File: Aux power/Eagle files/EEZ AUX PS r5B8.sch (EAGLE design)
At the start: 74 parts, among them IC1 LM25575, IC2 MC7812, IC3 TPD4E002DRLR, IC4 TPD2E001DZDR, IC5 ADUM3160BRWZ, Q1 BTA26-600, Q2 BTA26-600, Q3 IRLL014N, X1 282836-5, X2 09185067324, X3 22-23-2031, X4 LMJ2138812S0LOT6C, X5 826629-8, X6 826629-5, X7 SSW-105-02-S-S, X8 2411-01

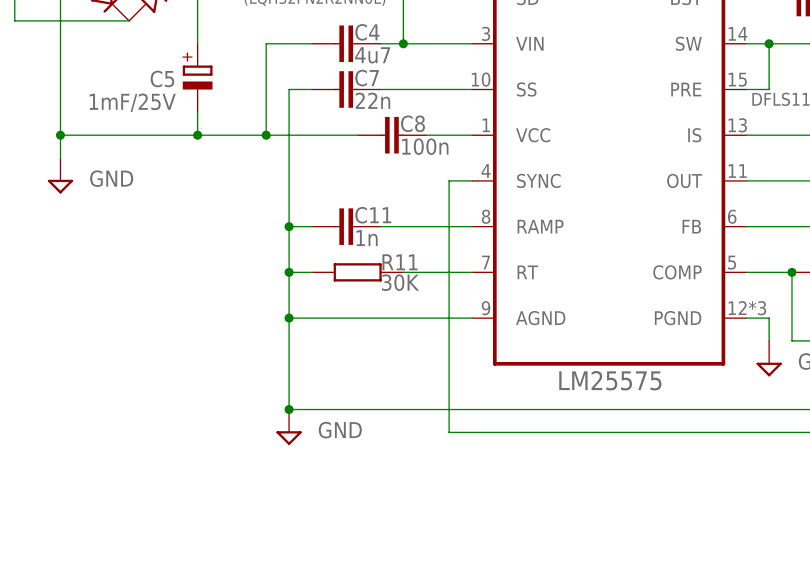
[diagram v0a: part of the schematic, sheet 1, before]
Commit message: Rt value corrections for AUX PS and Power board
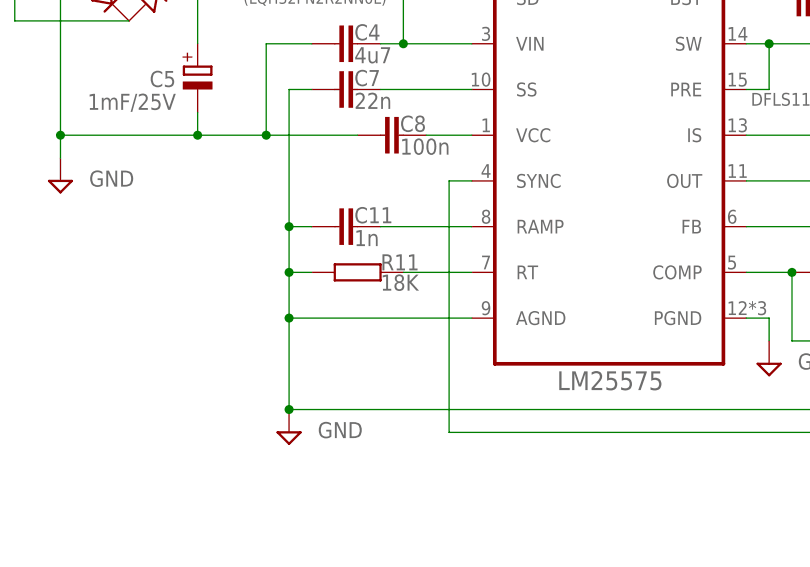
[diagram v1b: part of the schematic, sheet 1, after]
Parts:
- R11: value 30K -> 18K
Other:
- note removed: "Note 1.1: replace with 33K or 36K (to decrease frequency) if sync with power board is required"
- note removed: "See note 1.1"
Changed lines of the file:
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@@
 <part name="B1" library="rectifier" deviceset="DF*S" device="" technology="01" value="DF01S"/>
 <part name="C11" library="rcl" deviceset="C-EU" device="C0805" value="1n"/>
-<part name="R11" library="rcl" deviceset="R-EU_" device="R0805" value="30K"/>
+<part name="R11" library="rcl" deviceset="R-EU_" device="R0805" value="18K"/>
 <part name="R12" library="rcl" deviceset="R-EU_" device="R0805" value="20K"/>
 <part name="C12" library="rcl" deviceset="C-EU" device="C0805" value="3n9"/>
@@
 <text x="164.465" y="29.845" size="2.54" layer="94" font="vector">AC input protection, in-rush current limiter</text>
 <text x="164.465" y="26.035" size="2.54" layer="94" font="vector">+5V/1A power supply</text>
-<text x="6.985" y="15.24" size="1.27" layer="103">Note 1.1: replace with 33K or 36K (to decrease frequency) if sync with power board is required</text>
-<text x="92.71" y="55.88" size="1.27" layer="103">See note 1.1</text>
 <text x="12.7" y="165.735" size="1.778" layer="97" rot="R180">Line in</text>
 <text x="12.7" y="138.43" size="1.778" layer="97" rot="R180">Neutral in</text>

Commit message: AUX PS renumbering
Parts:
- removed R17: 5K6, rcl:R-EU_R0805
- removed R18: 10K, rcl:R-EU_R0805
- removed X1: 282836-5, EEZ_Lib1:TBLOCK5.0_5A
- removed X2: 09185067324, EEZ_Lib1:IDC-10PINBLACK
- removed X3: 22-23-2031, con-molex:22-23-2031
- added C97: 10u, MyLib6:ECAPPANASONIC_C
- added D21: BAS316, diode:DIODE-SOD323-W
- added R118: 5K6, rcl:R-EU_R0805
- added R119: 10K, rcl:R-EU_R0805
- added X10, X9: 826629-5, con-samtec:SSW-105-02-S-S
- added X11: 2411-01, con-kycon:KUSBVX-BS1N
- FB6, FB7: value 2506033007Y3 -> 60R@100MHz
- TR2: value TEZ6/D230/15V -> TEZ6/D230/12V
- X4: value LMJ2138812S0LOT6C -> 282836-5; device EEZ_Lib1:RJ45-VERT -> EEZ_Lib1:TBLOCK5.0_5A
- X5: value 826629-8 -> 09185067324; device con-samtec:SSW-108-02-S-S -> EEZ_Lib1:IDC-10PINBLACK; TME (none) -> T821-1-10-S1
- X6: value 826629-5 -> 22-23-2031; device con-samtec:SSW-105-02-S-S -> con-molex:22-23-2031
- X7: value SSW-105-02-S-S -> LMJ2138812S0LOT6C; device con-samtec:SSW-105-02-S-S -> EEZ_Lib1:RJ45-VERT
- X8: value 2411-01 -> 826629-8; device con-kycon:KUSBVX-BS1N -> con-samtec:SSW-108-02-S-S
- renumbered C1 to C84, C10 to C93, C11 to C94, C12 to C95, C13 to C96, C14 to C98, C15 to C99, C16 to C100, C17 to C101, C18 to C102, C19 to C103, C2 to C85, C20 to C104, C3 to C86, C4 to C87, C5 to C88, C6 to C89, C7 to C90, C8 to C91, C9 to C92, D1 to D19, D2 to D20, IC1 to IC16, IC2 to IC17, IC3 to IC18, IC4 to IC19, IC5 to IC20, L1 to L8, L2 to L9, L3 to FB5, L4 to L10, L5 to FB6, L6 to FB7, Q1 to Q20, Q2 to Q21, Q3 to Q22, R1 to R102, R10 to R111, R11 to R112, R12 to R113, R13 to R114, R14 to R115, R15 to R116, R16 to R117, R19 to R120, R2 to R103, R20 to R121, R3 to R104, R4 to R105, R5 to R106, R6 to R107, R7 to R108, R8 to R109, R9 to R110, TR1 to TR2, ZD1 to ZD6, ZD2 to ZD7
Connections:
- net DC_PREG1 renamed DC_PREG2
- net IS renamed IS1
- net SW renamed SW2
- removed net +3V3: FB5.2, X5-8.1
- removed net AC_IN1: C84.1, Q20.A1, Q21.A1, TR2.P2, VAR1.P$2, X1-1.1, ZD7.2
- removed net AC_IN2: C84.2, C85.1, TR2.P1, VAR2.P$1, X1-2.1, X1-4.1, ZD6.2
- removed net ETH_ACTLED: X4.YELLOW_A, X5-2.1
- removed net ETH_IN+: IC18.IO4, X4.RD-, X5-4.1
- removed net ETH_IN-: IC18.IO3, X4.RD+, X5-5.1
- removed net ETH_LINKLED: X4.GREEN-A, X5-1.1
- removed net ETH_OUT+: IC18.IO2, X4.TD-, X5-6.1
- removed net ETH_OUT-: IC18.IO1, X4.TD+, X5-7.1
- removed net FAN_CONTROL: R115.2, X2-6.1
- removed net FAN_SENSE: R17.2, R18.1, X2-5.1, X3-3.S
- removed net N$11: Q21.A2, R102.2, R103.2, R105.1, X1-3.1
- removed net N$13: IC16.SYNC, X2-7.1
- removed net N$21: C98.-, L10.1, X3-2.S
- removed net PWR_DIRECT: R104.2, X2-3.1
- removed net PWR_SSTART: R107.2, X2-4.1
- new net AC_IN1_MAIN: C84.1, Q20.A1, Q21.A1, TR2.P2, VAR1.P$2, X4-1.1, ZD7.2
- new net AC_IN2_MAIN: C84.2, C85.1, TR2.P1, VAR2.P$1, X4-2.1, X4-4.1, ZD6.2
- new net AUX_+3V3: FB5.2, X8-8.1
- new net AUX_ETH_ACTLED: X7.YELLOW_A, X8-2.1
- new net AUX_ETH_IN+: IC18.IO4, X7.RD-, X8-4.1
- new net AUX_ETH_IN-: IC18.IO3, X7.RD+, X8-5.1
- new net AUX_ETH_LINKLED: X7.GREEN-A, X8-1.1
- new net AUX_ETH_OUT+: IC18.IO2, X7.TD-, X8-6.1
- new net AUX_ETH_OUT-: IC18.IO1, X7.TD+, X8-7.1
- new net AUX_FAN_CTRL: R115.2, X5-6.1
- new net AUX_FAN_SENSE: D21.A, R118.2, R119.1, X5-5.1
- new net AUX_PWR_DIRECT: R104.2, X5-3.1
- new net AUX_PWR_SSTART: R107.2, X5-4.1
- new net N$163: D21.C, X6-3.S
- new net N$68: IC16.SYNC, X5-7.1
- new net N$82: Q21.A2, R102.2, R103.2, R105.1, X4-3.1
- new net N$86: C98.-, L10.1, X6-2.S
- net +5V: now also R118.1, X5-10.1, X5-8.1; no longer R17.1, X2-10.1, X2-8.1
- net 12VDC: now also C97.+, X6-1.S; no longer X3-1.S
- net AC_EARTH: now also X11.S1, X11.S2, X4-5.1, X7.SH, X9-5.1; no longer X1-5.1, X4.SH, X6-5.1, X8.S1, X8.S2
- net D+: now also X11.3, X9-3.1; no longer X6-3.1, X8.3
- net D-: now also X11.2, X9-2.1; no longer X6-2.1, X8.2
- net GND: now also C97.-, R119.2, X5-1.1, X5-2.1, X5-9.1, X7.GREEN-C, X7.YELLOW-C; no longer R18.2, X2-1.1, X2-2.1, X2-9.1, X4.GREEN-C, X4.YELLOW-C
- net MCU_D+: now also X10-3.1; no longer X7-3.1
- net MCU_D-: now also X10-2.1; no longer X7-2.1
- net N$125: now also X7.CT; no longer X4.CT
- net XUSB_GND: now also X11.4, X9-4.1; no longer X6-4.1, X8.4
- net XUSB_VBUS: now also X11.1, X9-1.1; no longer X6-1.1, X8.1
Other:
- note added: "10-pin IDC connector X5"
- note added: "3-pin connector X6"
- note added: "5-pin connector X9, X10"
- note added: "5-pin power connector X4"
- note added: "8-pin connector X8"
- note added: "Digikey: 237-1085-ND"
- note added: "Fan+ (Red) 1"
- note added: "Fan- (Black) 2"
- note added: "Mouser: 553-VPP24-210"
- note added: "Newark: 93F8764"
- note removed: "10-pin IDC connector X2"
- note removed: "3-pin connector X4"
- note removed: "5-pin connector X6, X7"
- note removed: "5-pin power connector X1"
- note removed: "8-pin connector X5"
- note removed: "Digikey: 237-1086-ND"
- note removed: "Fan + (Red) 1"
- note removed: "Fan - (Black) 2"
- note removed: "Mouser: 553-VPP28-180"
- note removed: "Newark: 37B9209"

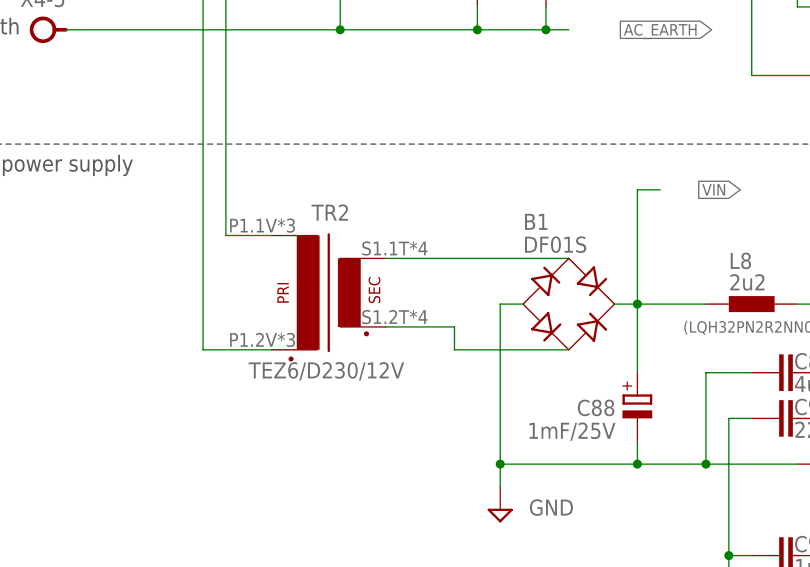
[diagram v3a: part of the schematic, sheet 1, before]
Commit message: Myrra AC/DC module for 115VAC, BOM updated
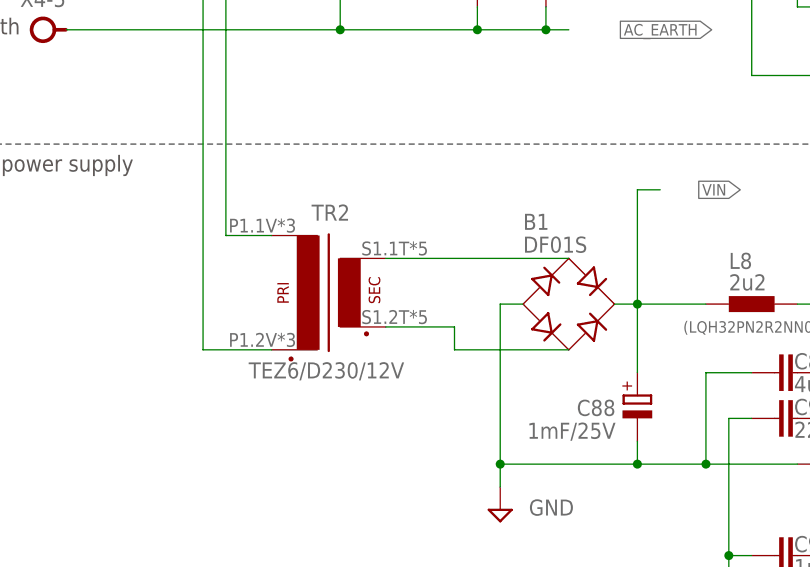
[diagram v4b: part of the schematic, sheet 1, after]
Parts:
- TR2: device EEZ_Lib1:PCB_TRAFO6VA_TEZ+VPP -> EEZ_Lib1:PCB_TRAFO6VA_TEZ+VPP+MYRRA
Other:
- note added: "Farnell: 2469211"
- note added: "Myrra 47202"
- note added: "TR2"
- note added: "VPP24-210"
- note added: "or AC/DC module"
- note removed: "TR1"
- note removed: "VPP28-180"
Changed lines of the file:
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@@
 <part name="R119" library="rcl" deviceset="R-EU_" device="R0805" value="10K"/>
 <part name="SUPPLY51" library="supply2" deviceset="GND" device=""/>
-<part name="TR2" library="EEZ_Lib1" deviceset="PCB_TRAFO6VA_TEZ+VPP" device="" value="TEZ6/D230/12V"/>
+<part name="TR2" library="EEZ_Lib1" deviceset="PCB_TRAFO6VA_TEZ+VPP" device="+MYRRA" value="TEZ6/D230/12V"/>
 <part name="VAR1" library="EEZ_Lib1" deviceset="VARISTOR" device="" value="S20K250"/>
 <part name="VAR2" library="EEZ_Lib1" deviceset="VARISTOR" device="" value="S20K250"/>
@@
 <text x="6.985" y="176.53" size="1.778" layer="97" rot="MR180">AC input protection and soft-start/stand-by</text>
 <text x="10.16" y="157.48" size="1.778" layer="103">AC input (230V)</text>
-<text x="9.525" y="34.925" size="1.6764" layer="103">SAR1</text>
-<text x="9.525" y="24.765" size="1.6764" layer="103">VAR1, VAR2</text>
-<text x="9.525" y="22.225" size="1.6764" layer="103">ZD1, ZD2</text>
-<text x="44.45" y="38.1" size="1.6764" layer="103">Code</text>
-<text x="26.67" y="38.1" size="1.6764" layer="103">Value</text>
-<text x="26.67" y="34.925" size="1.6764" layer="103">2027-23-BLF</text>
-<text x="44.45" y="34.925" size="1.6764" layer="103">Farnell: 1780455, TME: CG2-230L</text>
-<text x="26.67" y="24.765" size="1.6764" layer="103">S20K140</text>
-<text x="26.67" y="32.385" size="1.6764" layer="103">VPP28-180</text>
-<text x="44.45" y="27.305" size="1.6764" layer="103">Newark: 93F8764</text>
-<text x="44.45" y="24.765" size="1.6764" layer="103">Farnell: 1004387, TME: SIOV-S20K140</text>
-<wire x1="7.62" y1="40.64" x2="25.4" y2="40.64" width="0.1524" layer="103"/>
-<wire x1="25.4" y1="40.64" x2="43.18" y2="40.64" width="0.1524" layer="103"/>
-<wire x1="43.18" y1="40.64" x2="87.63" y2="40.64" width="0.1524" layer="103"/>
-<wire x1="87.63" y1="40.64" x2="87.63" y2="37.465" width="0.1524" layer="103"/>
-<wire x1="87.63" y1="37.465" x2="87.63" y2="21.59" width="0.1524" layer="103"/>
-<wire x1="87.63" y1="21.59" x2="43.18" y2="21.59" width="0.1524" layer="103"/>
-<wire x1="43.18" y1="21.59" x2="25.4" y2="21.59" width="0.1524" layer="103"/>
-<wire x1="25.4" y1="21.59" x2="7.62" y2="21.59" width="0.1524" layer="103"/>
-<wire x1="7.62" y1="21.59" x2="7.62" y2="37.465" width="0.1524" layer="103"/>
-<wire x1="7.62" y1="37.465" x2="7.62" y2="40.64" width="0.1524" layer="103"/>
-<wire x1="25.4" y1="21.59" x2="25.4" y2="40.64" width="0.1524" layer="103"/>
-<wire x1="43.18" y1="21.59" x2="43.18" y2="40.64" width="0.1524" layer="103"/>
-<wire x1="7.62" y1="37.465" x2="87.63" y2="37.465" width="0.1524" layer="103"/>
-<text x="9.525" y="38.1" size="1.6764" layer="103">Name</text>
-<text x="6.985" y="41.91" size="1.6764" layer="103">115VAC option:</text>
-<text x="9.525" y="32.385" size="1.6764" layer="103">TR1</text>
-<text x="26.67" y="22.225" size="1.6764" layer="103">1.5KE200CA</text>
-<text x="44.45" y="22.225" size="1.6764" layer="103">Farnell: 1837117, TME: 1.5KE200CA</text>
-<text x="44.45" y="32.385" size="1.6764" layer="103">Digikey: 237-1085-ND</text>
-<text x="44.45" y="29.845" size="1.6764" layer="103">Mouser: 553-VPP24-210</text>
 <circle x="232.41" y="67.31" radius="0.635" width="0.1524" layer="101"/>
 <circle x="232.41" y="69.85" radius="0.635" width="0.1524" layer="101"/>
@@
 <text x="2.54" y="152.4" size="1.4224" layer="103">or Schurter KM00.1105.11 IEC intlet</text>
 <text x="2.54" y="149.86" size="1.4224" layer="103">with Schurter 4301.1403 fuse drawer</text>
+<text x="6.985" y="34.925" size="1.6764" layer="103">SAR1</text>
+<text x="6.985" y="19.685" size="1.6764" layer="103">VAR1, VAR2</text>
+<text x="6.985" y="17.145" size="1.6764" layer="103">ZD1, ZD2</text>
+<text x="44.45" y="38.1" size="1.6764" layer="103">Code</text>
+<text x="24.13" y="38.1" size="1.6764" layer="103">Value</text>
+<text x="24.13" y="34.925" size="1.6764" layer="103">2027-23-BLF</text>
+<text x="44.45" y="34.925" size="1.6764" layer="103">Farnell: 1780455, TME: CG2-230L</text>
+<text x="24.13" y="19.685" size="1.6764" layer="103">S20K140</text>
+<text x="24.13" y="32.385" size="1.6764" layer="103">VPP24-210</text>
+<text x="44.45" y="19.685" size="1.6764" layer="103">Farnell: 1004387, TME: SIOV-S20K140</text>
+<wire x1="5.08" y1="40.64" x2="22.86" y2="40.64" width="0.1524" layer="103"/>
+<wire x1="22.86" y1="40.64" x2="43.18" y2="40.64" width="0.1524" layer="103"/>
+<wire x1="43.18" y1="40.64" x2="87.63" y2="40.64" width="0.1524" layer="103"/>
+<wire x1="87.63" y1="40.64" x2="87.63" y2="37.465" width="0.1524" layer="103"/>
+<wire x1="87.63" y1="37.465" x2="87.63" y2="16.51" width="0.1524" layer="103"/>
+<wire x1="87.63" y1="16.51" x2="43.18" y2="16.51" width="0.1524" layer="103"/>
+<wire x1="43.18" y1="16.51" x2="22.86" y2="16.51" width="0.1524" layer="103"/>
+<wire x1="22.86" y1="16.51" x2="5.08" y2="16.51" width="0.1524" layer="103"/>
+<wire x1="5.08" y1="16.51" x2="5.08" y2="37.465" width="0.1524" layer="103"/>
+<wire x1="5.08" y1="37.465" x2="5.08" y2="40.64" width="0.1524" layer="103"/>
+<wire x1="22.86" y1="16.51" x2="22.86" y2="40.64" width="0.1524" layer="103"/>
+<wire x1="43.18" y1="16.51" x2="43.18" y2="40.64" width="0.1524" layer="103"/>
+<wire x1="5.08" y1="37.465" x2="87.63" y2="37.465" width="0.1524" layer="103"/>
+<text x="6.985" y="38.1" size="1.6764" layer="103">Name</text>
+<text x="4.445" y="41.91" size="1.6764" layer="103">115VAC option:</text>
+<text x="6.985" y="32.385" size="1.6764" layer="103">TR2</text>
+<text x="24.13" y="17.145" size="1.6764" layer="103">1.5KE200CA</text>
+<text x="44.45" y="17.145" size="1.6764" layer="103">Farnell: 1837117, TME: 1.5KE200CA</text>
+<text x="44.45" y="22.225" size="1.6764" layer="103">Farnell: 2469211</text>
+<text x="44.45" y="32.385" size="1.6764" layer="103">Digikey: 237-1085-ND</text>
+<text x="44.45" y="29.845" size="1.6764" layer="103">Mouser: 553-VPP24-210</text>
+<text x="24.13" y="24.765" size="1.6764" layer="103">or AC/DC module</text>
+<text x="44.45" y="27.305" size="1.6764" layer="103">Newark: 93F8764</text>
+<text x="24.13" y="22.225" size="1.6764" layer="103">Myrra 47202</text>
 </plain>
 <instances>
